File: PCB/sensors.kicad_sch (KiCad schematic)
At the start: 16 parts, among them U5 BME280, U7 TLC555xPS

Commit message: Updated some component packages
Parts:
- removed U7: TLC555xPS, Package_SO:VSSOP-8_3x3mm_P0.65mm, symbol Timer:TLC555xPS
- added U9: TLC555xD, Package_SO:SOIC-8_3.9x4.9mm_P1.27mm, symbol Timer:TLC555xD
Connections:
- net +3.3V: now also U9.4 (R), U9.8 (VCC)
- net GND: now also U9.1 (GND)
- net Q: now also U9.3 (Q)
- net at R14.1, R16.1: now also U9.7 (DIS)
- net at C25.1, R16.2: now also U9.2 (TR), U9.6 (THR)
- net at C23.1: now also U9.5 (CV)

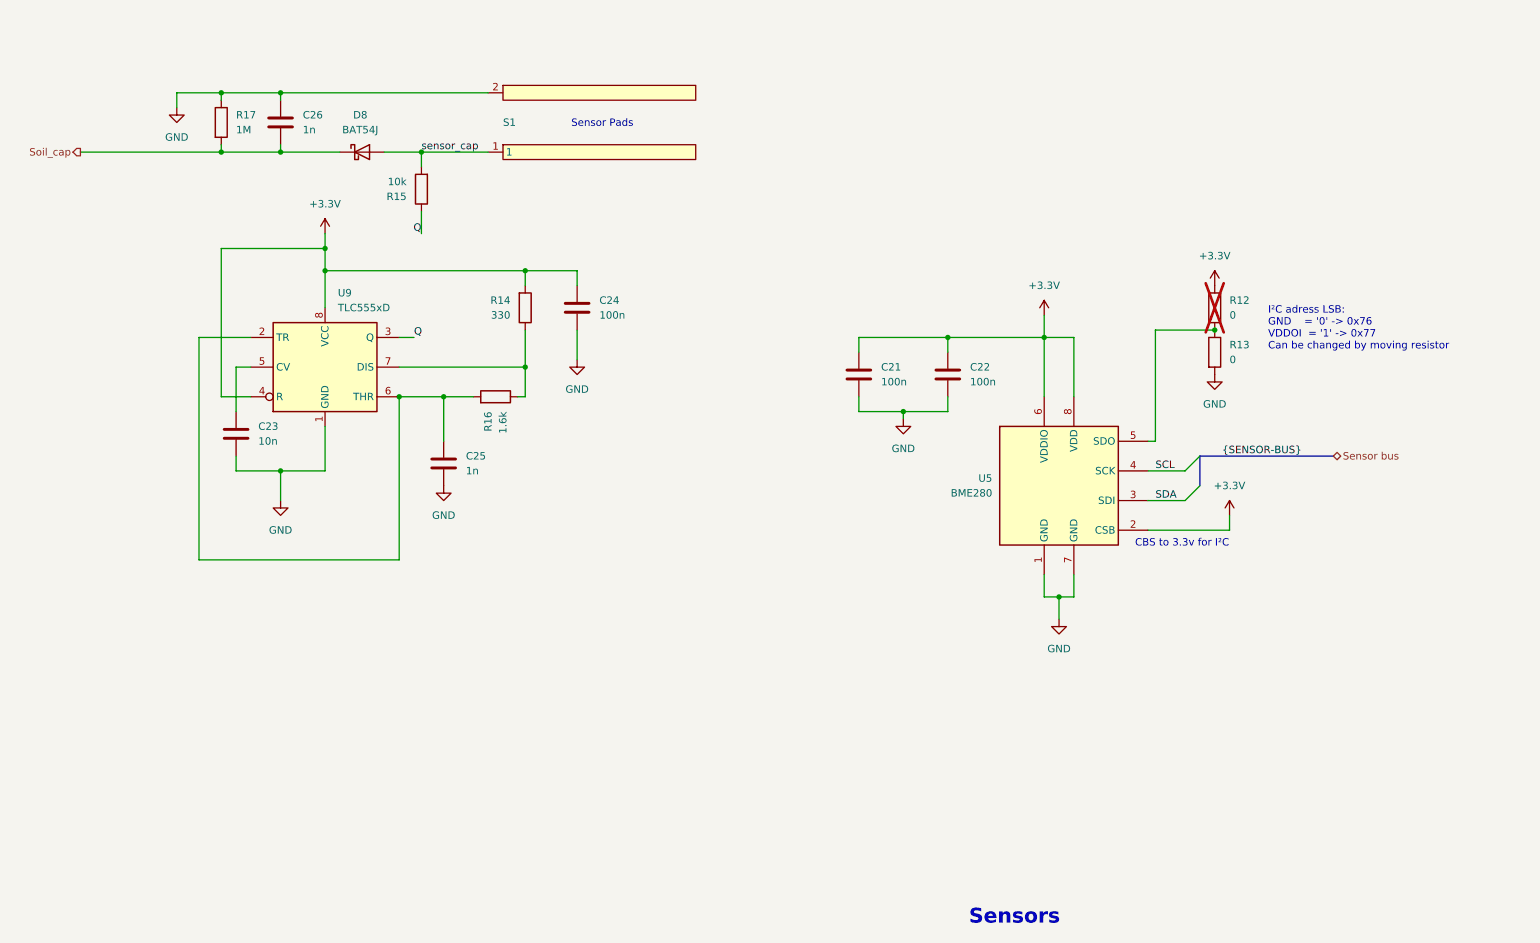
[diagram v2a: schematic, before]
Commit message: Added light sensor simulation and schematic
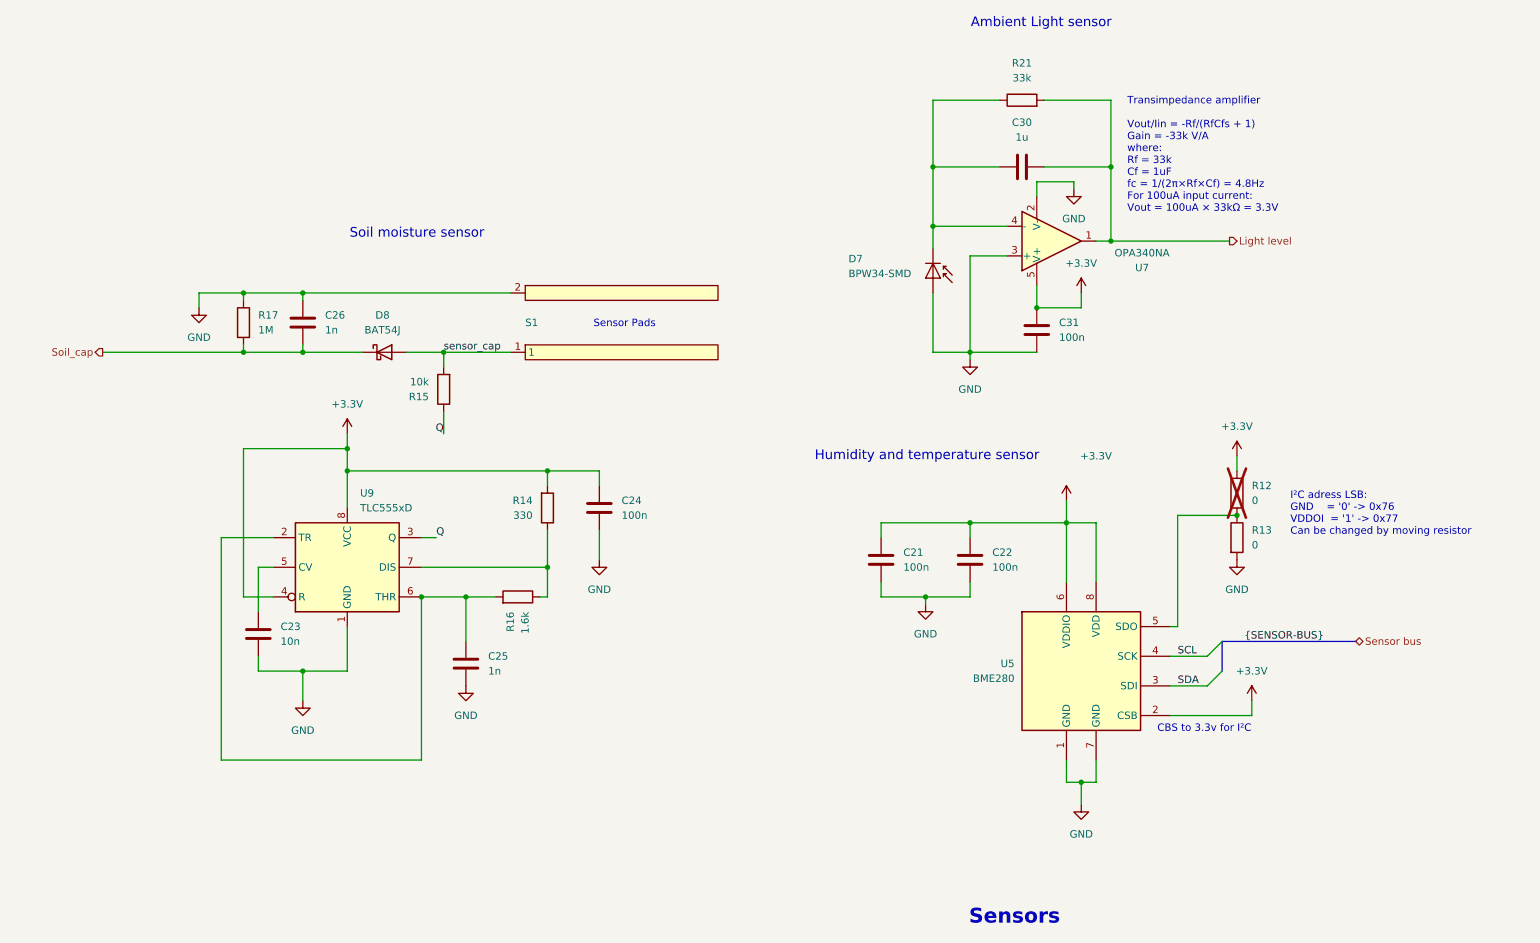
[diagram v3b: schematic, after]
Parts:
- added C30: 1u, Capacitor_SMD:C_0603_1608Metric, symbol Device:C
- added C31: 100n, Capacitor_SMD:C_0402_1005Metric, symbol Device:C
- added D7: BPW34-SMD, OptoDevice:Osram_BPW34S-SMD, symbol Sensor_Optical:BPW34-SMD
- added R21: 33k, Resistor_SMD:R_0402_1005Metric, symbol Device:R
- added U7: OPA340NA, Package_TO_SOT_SMD:SOT-23-5, symbol Amplifier_Operational:OPA340NA
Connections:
- net +3.3V: now also C31.1, U7.5 (V+)
- net GND: now also C31.2, D7.2 (A), U7.2 (V-), U7.3 (+)
- new net: C30.1, D7.1 (K), R21.1, U7.4 (-)
- new net Light level: C30.2, R21.2, U7.1
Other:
- note added: "Ambient Light sensor"
- note added: "Humidity and temperature sensor"
- note added: "Soil moisture sensor"
- note added: "Transimpedance amplifier Vout/Iin = -Rf/(RfCfs + 1) Gain = -33k V/A where: Rf = 33k Cf = 1uF fc = 1/(2π×Rf×Cf) = 4.8Hz For 100uA input current: Vout = 100uA × 33kΩ = 3.3V"
- moved on the sheet: C21, C22, C23, C24, C25, C26, D8, R12, R13, R14, R15, R16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

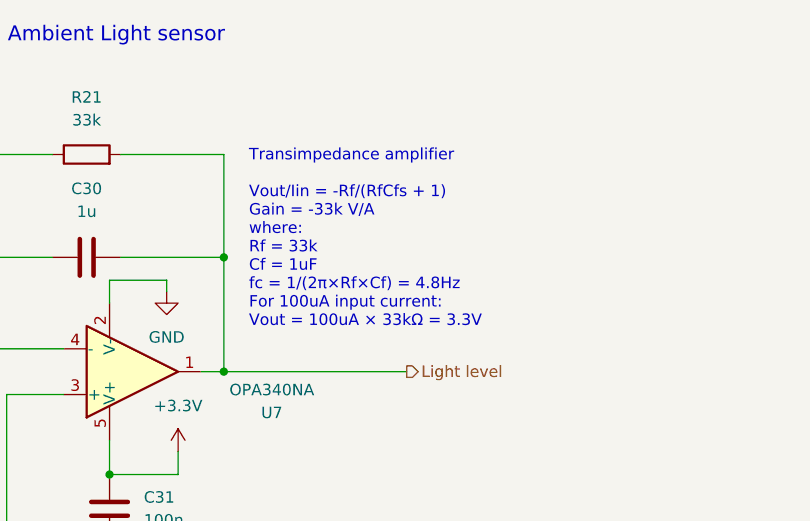
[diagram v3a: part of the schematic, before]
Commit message: removed usb port library
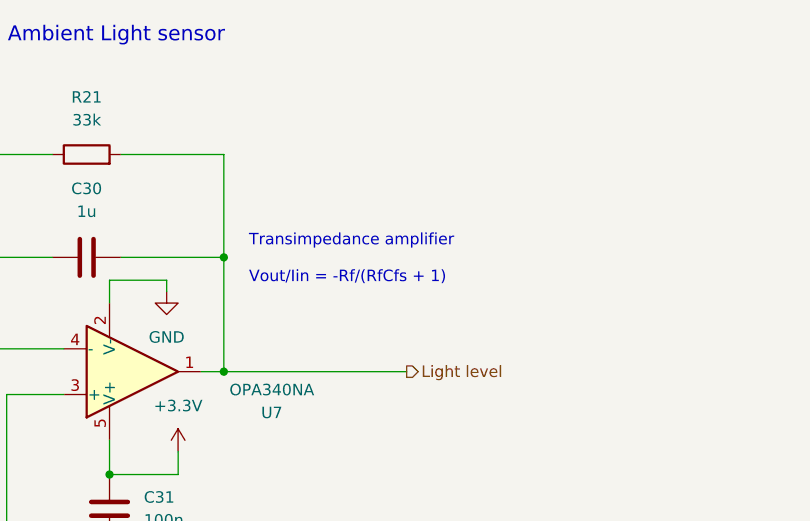
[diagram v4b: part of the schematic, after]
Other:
- note added: "Transimpedance amplifier Vout/Iin = -Rf/(RfCfs + 1)"
- note removed: "Transimpedance amplifier Vout/Iin = -Rf/(RfCfs + 1) Gain = -33k V/A where: Rf = 33k Cf = 1uF fc = 1/(2π×Rf×Cf) = 4.8Hz For 100uA input current: Vout = 100uA × 33kΩ = 3.3V"
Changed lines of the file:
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@@
 		)
 	)
-	(text "Transimpedance amplifier\n\nVout/Iin = -Rf/(RfCfs + 1)\nGain = -33k V/A\nwhere:\nRf = 33k\nCf = 1uF\nfc = 1/(2π×Rf×Cf) = 4.8Hz\nFor 100uA input current:\nVout = 100uA × 33kΩ = 3.3V"
+	(text "Transimpedance amplifier\n\nVout/Iin = -Rf/(RfCfs + 1)"
 		(exclude_from_sim no)
-		(at 208.534 43.688 0)
+		(at 208.534 45.974 0)
 		(effects
 			(font
